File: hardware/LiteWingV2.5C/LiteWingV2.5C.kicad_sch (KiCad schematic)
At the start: 87 parts, among them IC1 TP4056, J1 USB_C_Receptacle_USB2.0, J10 Conn_01x02_Female, J11 Conn_01x09, J12 Conn_01x06, J13 Conn_01x07, J14 Conn_01x02, J2 JST XH 2P 2.50mm SMD Hoz, J3 Conn_01x06, J4 Conn_01x06, J5 Conn_01x06, J6 Conn_01x06, J7 Conn_01x02_Female, J8 Conn_01x02_Female, J9 Conn_01x02_Female, SW1 MST22D18G2_125, SW2 Tactile Switch 3x4x2, SW3 Tactile Switch 3x4x2, T1 IRLML6344TRPBF, T2 IRLML6344TRPBF, T3 IRLML6344TRPBF, T4 IRLML6344TRPBF, U1 AO3401A, U2 SPX3819M5-L-3-3/TR, U5 CH340K, U6 2N27002DW, U7 MPU-6050, U8 ESP32-S3-WROOM-1

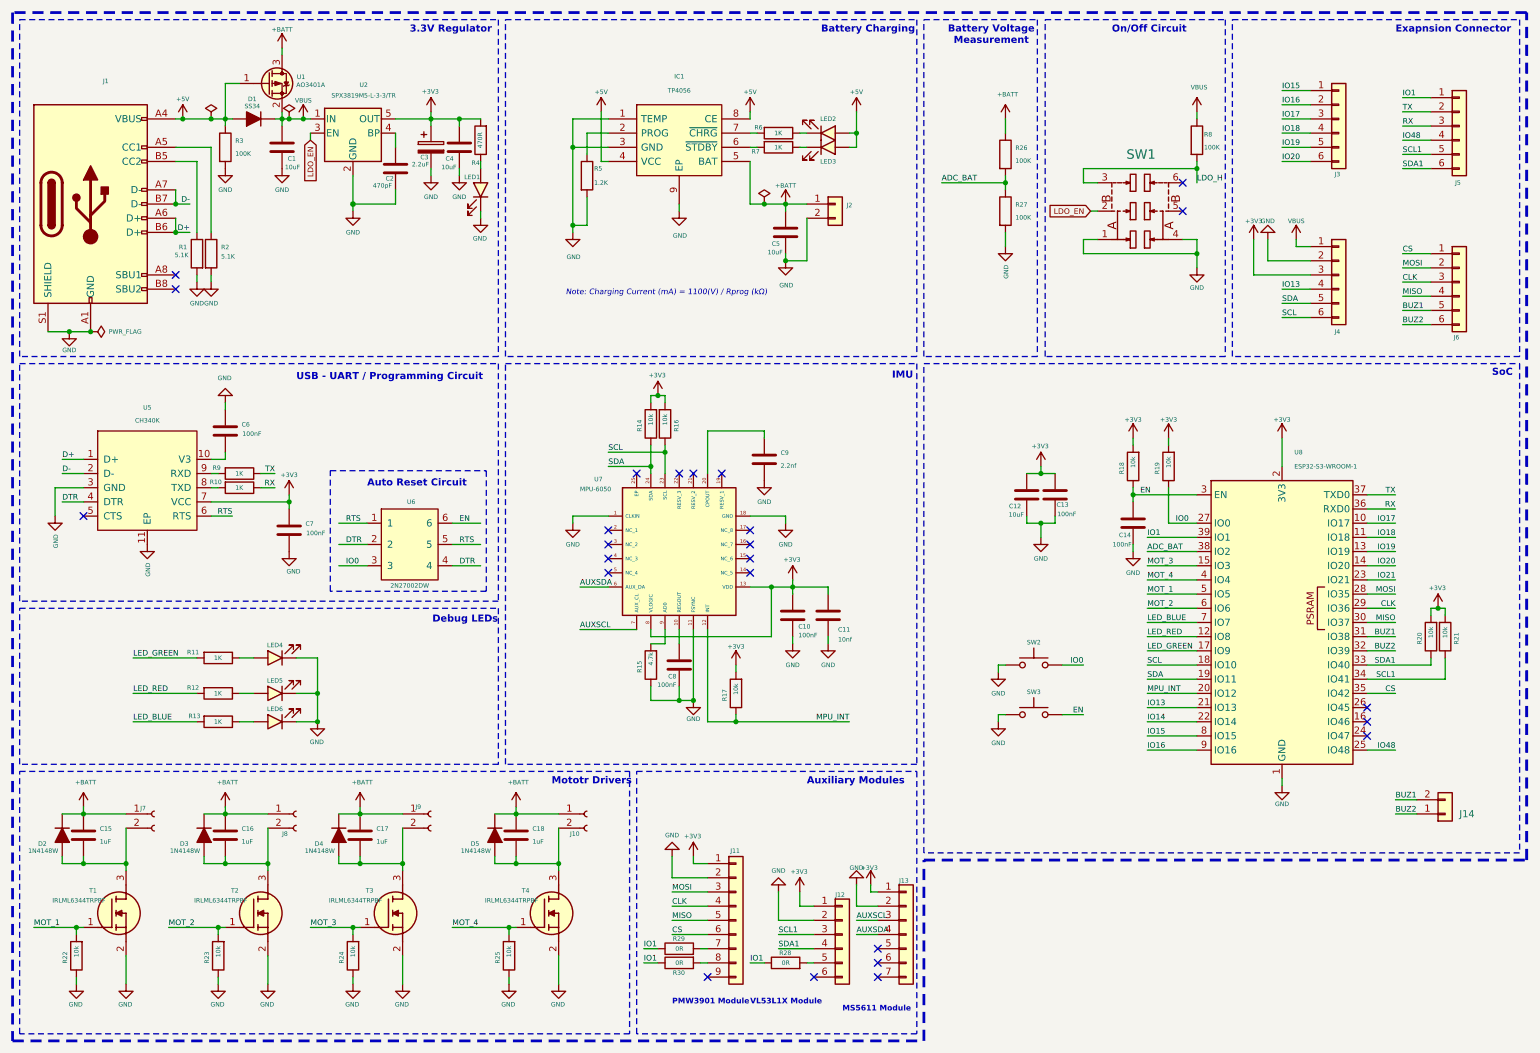
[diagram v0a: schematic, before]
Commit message: Update to remove USB to serial converter and use native USB on ESP32-S3 instead.
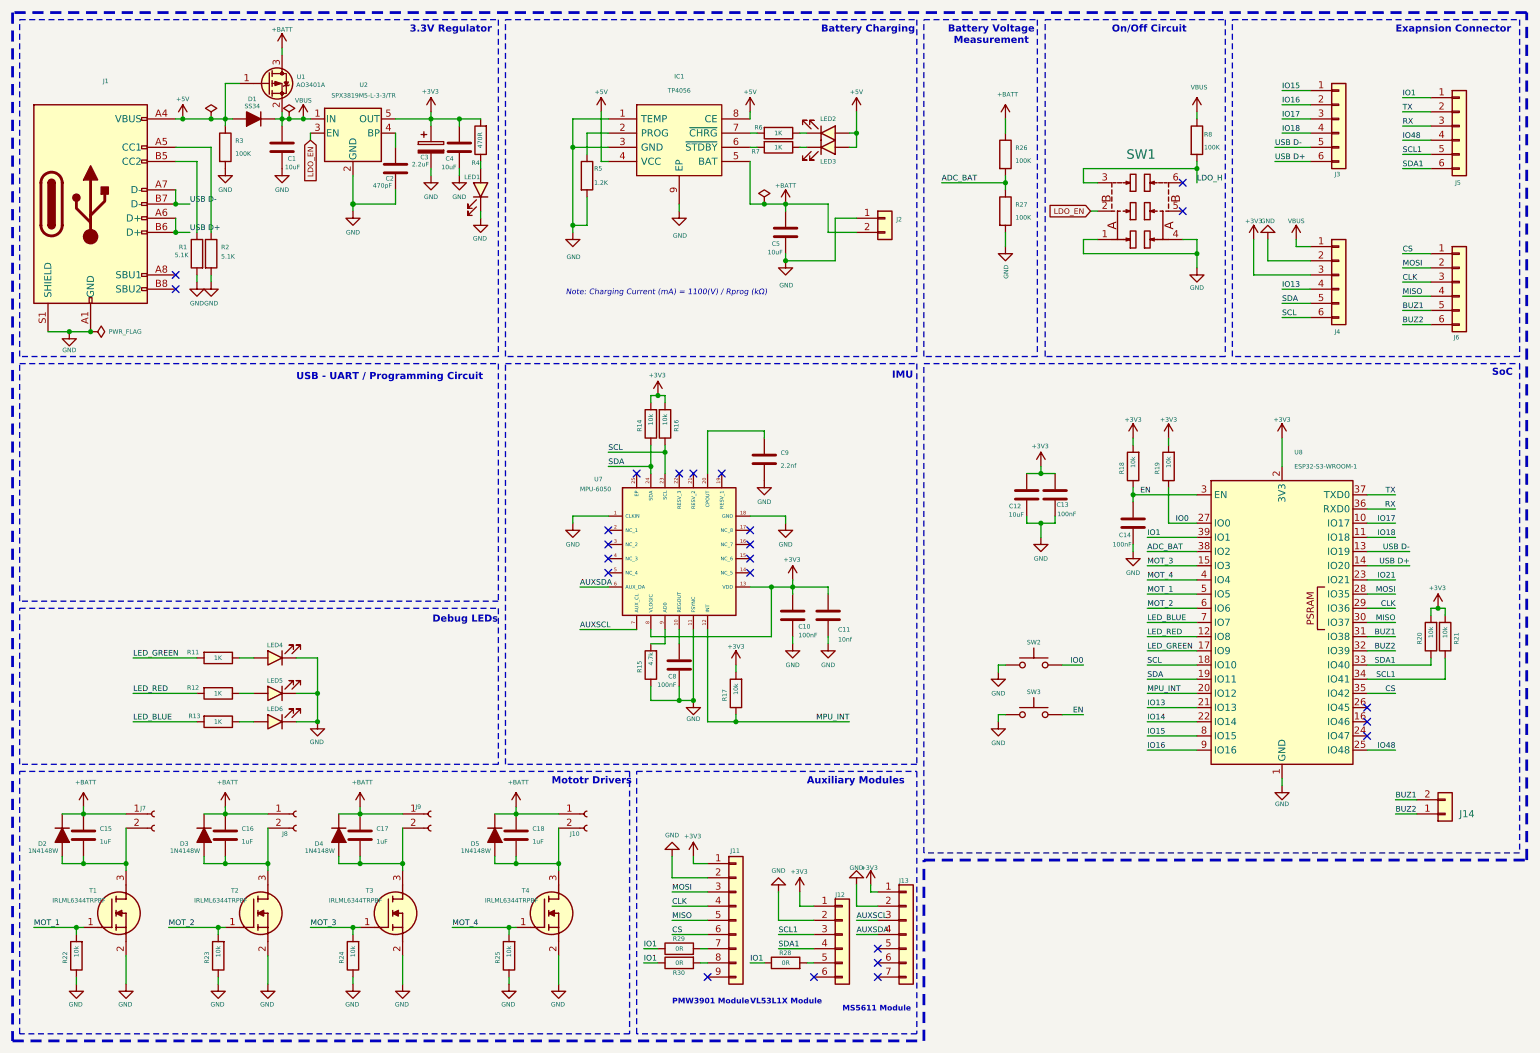
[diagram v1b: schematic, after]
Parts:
- removed C6, C7: 100nF, Capacitor_SMD:C_0603_1608Metric, symbol Device:C
- removed R10, R9: 1K, Resistor_SMD:R_0603_1608Metric, symbol Device:R
- removed U5: CH340K, ch340k:ESSOP-10_3.9x4.9mm_P1.00mm, symbol downloader-rescue:ch340k-my
- removed U6: 2N27002DW, Package_TO_SOT_SMD:SOT-363_SC-70-6, symbol downloader-rescue:DDC114TU-7-F-my
- J1: value USB_C_Receptacle_USB2.0 -> USB_C_Receptacle_USB2.0_16P; footprint Connector_USB:USB_C_Receptacle_HRO_TYPE-C-31-M-12 -> SL_Power:USB_C_Receptacle_G-Switch_GT-USB-7010ASV; LCSC Link https://www.lcsc.com/product-detail/USB-Connectors_DEALON-U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 -> https://www.lcsc.com/product-detail/span-style-background-c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; LCSC Part # C2927038 -> C2988369; MFR.Part # USB-TYPE-C-018 -> (none); Manufacturer DEALON -> (none)
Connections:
- net IO19 is gone; now on net USB D-: J3.5 (Pin_5), U8.13 (IO19)
- net IO20 is gone; now on net USB D+: J3.6 (Pin_6), U8.14 (IO20)
- net +BATT: now also J2.2 (Pin_2); no longer J2.1 (Pin_1)
- net GND: now also J2.1 (Pin_1); no longer J2.2 (Pin_2)
- net D+ renamed USB D+
- net D- renamed USB D-
- no-connect marks 25 -> 24
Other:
- note removed: "Auto Reset Circuit"
- moved on the sheet: J2
